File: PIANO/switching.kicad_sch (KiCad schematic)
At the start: 7 parts, among them J3 Barrel_Jack_Switch, U5 AP1509-50SG-13

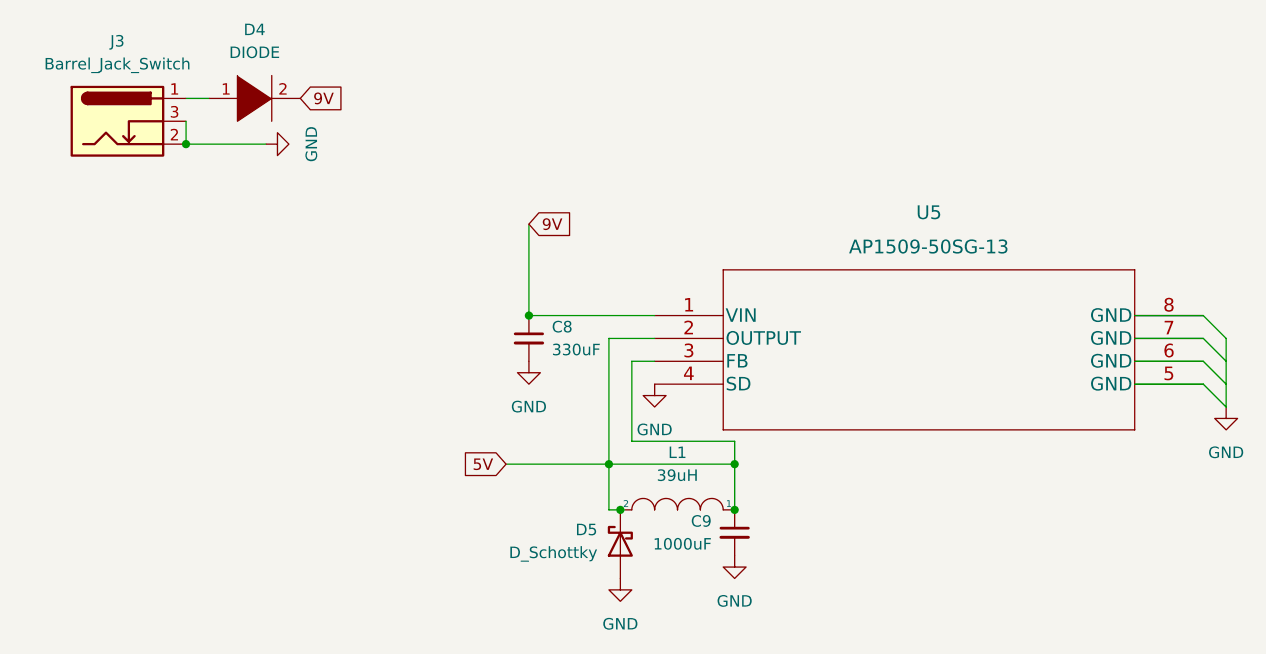
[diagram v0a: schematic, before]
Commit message: Bathroom Trip Commit
Did the circuit for most of the regulator
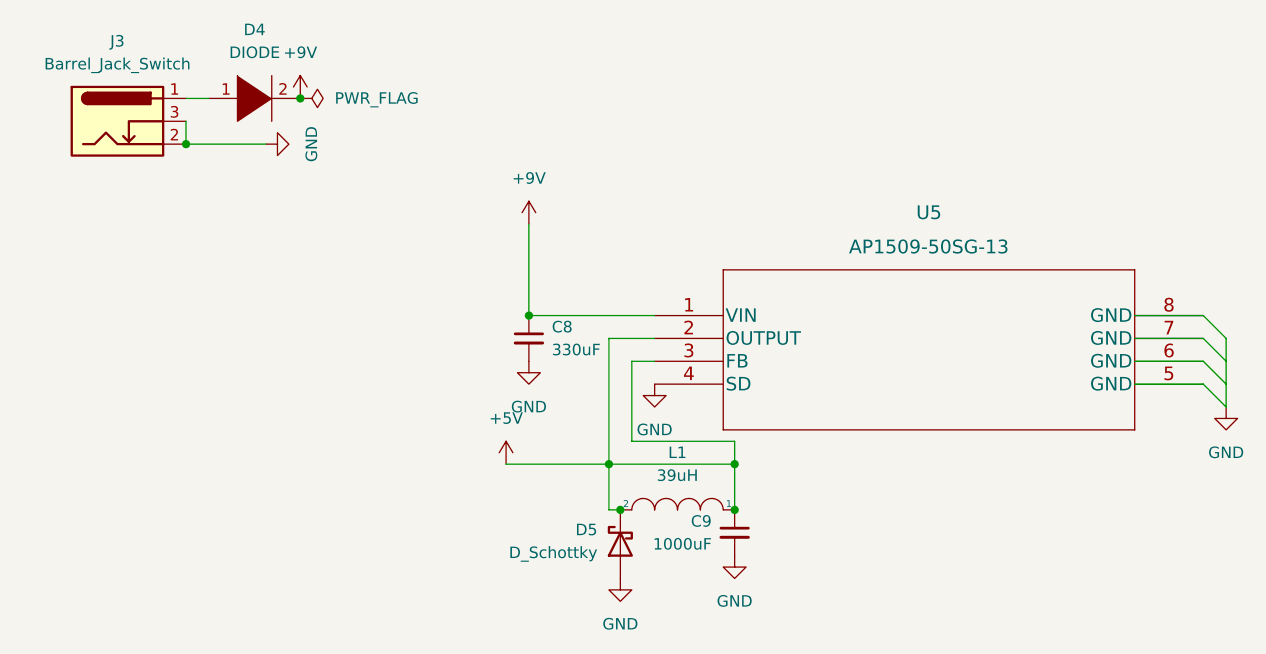
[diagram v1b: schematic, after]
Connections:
- net 5V renamed +5V
- net 9V renamed +9V
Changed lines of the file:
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@@
   (junction (at 129.54 104.14) (diameter 0) (color 0 0 0 0)
   )
+  (junction (at 81.28 58.42) (diameter 0) (color 0 0 0 0)
+  )
   (junction (at 129.54 99.06) (diameter 0) (color 0 0 0 0)
   )
@@
   (wire (pts (xy 129.54 96.52) (xy 118.11 96.52))
     (stroke (width 0) (type default) (color 0 0 0 0))
-  )
-  (global_label "5V" (shape input) (at 104.14 99.06 180) (fields_autoplaced)
-    (effects (font (size 1.27 1.27)) (justify right))
-    (property "Intersheet References" "${INTERSHEET_REFS}" (id 0) (at 99.4288 98.9806 0)
-      (effects (font (size 1.27 1.27)) (justify right) hide)
-    )
-  )
-  (global_label "9V" (shape input) (at 81.28 58.42 0) (fields_autoplaced)
-    (effects (font (size 1.27 1.27)) (justify left))
-    (property "Intersheet References" "${INTERSHEET_REFS}" (id 0) (at 85.9912 58.3406 0)
-      (effects (font (size 1.27 1.27)) (justify left) hide)
-    )
-  )
-  (global_label "9V" (shape input) (at 106.68 72.39 0) (fields_autoplaced)
-    (effects (font (size 1.27 1.27)) (justify left))
-    (property "Intersheet References" "${INTERSHEET_REFS}" (id 0) (at 111.3912 72.3106 0)
-      (effects (font (size 1.27 1.27)) (justify left) hide)
-    )
   )
   (symbol (lib_id "power:GND") (at 77.47 63.5 90) (unit 1)
@@
     )
     (property "Datasheet" "" (id 3) (at 77.47 63.5 0)
+      (effects (font (size 1.27 1.27)) hide)
+    )
+    (pin "1")
+  )
+  (symbol (lib_id "power:PWR_FLAG") (at 81.28 58.42 270) (unit 1)
+    (in_bom yes) (on_board yes) (fields_autoplaced)
+    (property "Reference" "#FLG0104" (id 0) (at 83.185 58.42 0)
+      (effects (font (size 1.27 1.27)) hide)
+    )
+    (property "Value" "PWR_FLAG" (id 1) (at 85.09 58.4199 90)
+      (effects (font (size 1.27 1.27)) (justify left))
+    )
+    (property "Footprint" "" (id 2) (at 81.28 58.42 0)
+      (effects (font (size 1.27 1.27)) hide)
+    )
+    (property "Datasheet" "~" (id 3) (at 81.28 58.42 0)
       (effects (font (size 1.27 1.27)) hide)
     )
@@
     (pin "2")
     (pin "3")
+  )
+  (symbol (lib_id "power:+5V") (at 104.14 99.06 0) (unit 1)
+    (in_bom yes) (on_board yes) (fields_autoplaced)
+    (property "Reference" "#PWR0132" (id 0) (at 104.14 102.87 0)
+      (effects (font (size 1.27 1.27)) hide)
+    )
+    (property "Value" "+5V" (id 1) (at 104.14 93.98 0))
+    (property "Footprint" "" (id 2) (at 104.14 99.06 0)
+      (effects (font (size 1.27 1.27)) hide)
+    )
+    (property "Datasheet" "" (id 3) (at 104.14 99.06 0)
+      (effects (font (size 1.27 1.27)) hide)
+    )
+    (pin "1")
   )
   (symbol (lib_id "power:GND") (at 120.65 90.17 0) (unit 1)
@@
     (pin "8")
   )
+  (symbol (lib_id "power:+9V") (at 81.28 58.42 0) (unit 1)
+    (in_bom yes) (on_board yes) (fields_autoplaced)
+    (property "Reference" "#PWR0136" (id 0) (at 81.28 62.23 0)
+      (effects (font (size 1.27 1.27)) hide)
+    )
+    (property "Value" "+9V" (id 1) (at 81.28 53.34 0))
+    (property "Footprint" "" (id 2) (at 81.28 58.42 0)
+      (effects (font (size 1.27 1.27)) hide)
+    )
+    (property "Datasheet" "" (id 3) (at 81.28 58.42 0)
+      (effects (font (size 1.27 1.27)) hide)
+    )
+    (pin "1")
+  )
   (symbol (lib_id "pspice:INDUCTOR") (at 123.19 104.14 0) (mirror y) (unit 1)
     (in_bom yes) (on_board yes) (fields_autoplaced)
@@
       (effects (font (size 1.27 1.27)) hide)
     )
+    (pin "1")
+  )
+  (symbol (lib_id "power:+9V") (at 106.68 72.39 0) (unit 1)
+    (in_bom yes) (on_board yes) (fields_autoplaced)
+    (property "Reference" "#PWR0137" (id 0) (at 106.68 76.2 0)
+      (effects (font (size 1.27 1.27)) hide)
+    )
+    (property "Value" "+9V" (id 1) (at 106.68 67.31 0))
+    (property "Footprint" "" (id 2) (at 106.68 72.39 0)
+      (effects (font (size 1.27 1.27)) hide)
+    )
+    (property "Datasheet" "" (id 3) (at 106.68 72.39 0)
+      (effects (font (size 1.27 1.27)) hide)
+    )

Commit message: fixed most things
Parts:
- C8: footprint Capacitor_SMD:C_1206_3216Metric -> Capacitor_SMD:C_1210_3225Metric
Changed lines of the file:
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@@
 (kicad_sch (version 20211123) (generator eeschema)
   (paper "A4")
+  (junction (at 106.68 76.2) (diameter 0) (color 0 0 0 0)
+  )
   (junction (at 115.57 99.06) (diameter 0) (color 0 0 0 0)
   )
@@
   (junction (at 106.68 82.55) (diameter 0) (color 0 0 0 0)
   )
+  (junction (at 95.25 96.52) (diameter 0) (color 0 0 0 0)
+  )
   (junction (at 129.54 104.14) (diameter 0) (color 0 0 0 0)
   )
@@
     (stroke (width 0) (type default) (color 0 0 0 0))
   )
-  (wire (pts (xy 106.68 72.39) (xy 106.68 82.55))
+  (wire (pts (xy 106.68 72.39) (xy 106.68 76.2))
     (stroke (width 0) (type default) (color 0 0 0 0))
   )
@@
     (stroke (width 0) (type default) (color 0 0 0 0))
   )
+  (wire (pts (xy 106.68 76.2) (xy 109.22 76.2))
+    (stroke (width 0) (type default) (color 0 0 0 0))
+  )
   (wire (pts (xy 68.58 63.5) (xy 77.47 63.5))
     (stroke (width 0) (type default) (color 0 0 0 0))
@@
     (stroke (width 0) (type default) (color 0 0 0 0))
   )
+  (wire (pts (xy 106.68 76.2) (xy 106.68 82.55))
+    (stroke (width 0) (type default) (color 0 0 0 0))
+  )
   (wire (pts (xy 184.15 90.17) (xy 184.15 92.71))
     (stroke (width 0) (type default) (color 0 0 0 0))
@@
     (stroke (width 0) (type default) (color 0 0 0 0))
   )
-  (wire (pts (xy 104.14 99.06) (xy 115.57 99.06))
+  (wire (pts (xy 95.25 99.06) (xy 115.57 99.06))
     (stroke (width 0) (type default) (color 0 0 0 0))
   )
@@
     (stroke (width 0) (type default) (color 0 0 0 0))
   )
+  (wire (pts (xy 95.25 96.52) (xy 95.25 93.98))
+    (stroke (width 0) (type default) (color 0 0 0 0))
+  )
   (wire (pts (xy 173.99 82.55) (xy 181.61 82.55))
     (stroke (width 0) (type default) (color 0 0 0 0))
   )
+  (wire (pts (xy 95.25 96.52) (xy 97.79 96.52))
+    (stroke (width 0) (type default) (color 0 0 0 0))
+  )
   (wire (pts (xy 129.54 99.06) (xy 129.54 96.52))
     (stroke (width 0) (type default) (color 0 0 0 0))
@@
     (stroke (width 0) (type default) (color 0 0 0 0))
   )
+  (wire (pts (xy 95.25 99.06) (xy 95.25 96.52))
+    (stroke (width 0) (type default) (color 0 0 0 0))
+  )
   (wire (pts (xy 118.11 87.63) (xy 120.65 87.63))
     (stroke (width 0) (type default) (color 0 0 0 0))
@@
   (wire (pts (xy 129.54 96.52) (xy 118.11 96.52))
     (stroke (width 0) (type default) (color 0 0 0 0))
+  )
+  (global_label "9V" (shape input) (at 109.22 76.2 0) (fields_autoplaced)
+    (effects (font (size 1.27 1.27)) (justify left))
+    (property "Intersheet References" "${INTERSHEET_REFS}" (id 0) (at 113.9312 76.1206 0)
+      (effects (font (size 1.27 1.27)) (justify left) hide)
+    )
+  )
+  (global_label "5V" (shape input) (at 97.79 96.52 0) (fields_autoplaced)
+    (effects (font (size 1.27 1.27)) (justify left))
+    (property "Intersheet References" "${INTERSHEET_REFS}" (id 0) (at 102.5012 96.4406 0)
+      (effects (font (size 1.27 1.27)) (justify left) hide)
+    )
   )
   (symbol (lib_id "power:GND") (at 77.47 63.5 90) (unit 1)
@@
     (pin "3")
   )
-  (symbol (lib_id "power:+5V") (at 104.14 99.06 0) (unit 1)
-    (in_bom yes) (on_board yes) (fields_autoplaced)
-    (property "Reference" "#PWR0132" (id 0) (at 104.14 102.87 0)
-      (effects (font (size 1.27 1.27)) hide)
-    )
-    (property "Value" "+5V" (id 1) (at 104.14 93.98 0))
-    (property "Footprint" "" (id 2) (at 104.14 99.06 0)
-      (effects (font (size 1.27 1.27)) hide)
-    )
-    (property "Datasheet" "" (id 3) (at 104.14 99.06 0)
+  (symbol (lib_id "power:+5V") (at 95.25 93.98 0) (unit 1)
+    (in_bom yes) (on_board yes)
+    (property "Reference" "#PWR0132" (id 0) (at 95.25 97.79 0)
+      (effects (font (size 1.27 1.27)) hide)
+    )
+    (property "Value" "+5V" (id 1) (at 92.71 90.17 0))
+    (property "Footprint" "" (id 2) (at 95.25 93.98 0)
+      (effects (font (size 1.27 1.27)) hide)
+    )
+    (property "Datasheet" "" (id 3) (at 95.25 93.98 0)
       (effects (font (size 1.27 1.27)) hide)
     )
@@
   )
   (symbol (lib_id "power:GND") (at 106.68 87.63 0) (unit 1)
-    (in_bom yes) (on_board yes) (fields_autoplaced)
+    (in_bom yes) (on_board yes)
     (property "Reference" "#PWR0130" (id 0) (at 106.68 93.98 0)
       (effects (font (size 1.27 1.27)) hide)
     )
-    (property "Value" "GND" (id 1) (at 106.68 92.71 0))
+    (property "Value" "GND" (id 1) (at 106.68 91.44 0))
     (property "Footprint" "" (id 2) (at 106.68 87.63 0)
       (effects (font (size 1.27 1.27)) hide)
@@
       (effects (font (size 1.27 1.27)) (justify left))
     )
-    (property "Footprint" "Capacitor_SMD:C_1206_3216Metric" (id 2) (at 106.68 85.09 0)
-      (effects (font (size 1.27 1.27)) hide)
-    )
+    (property "Footprint" "Capacitor_SMD:C_1210_3225Metric" (id 2) (at 106.68 85.09 0)
+      (effects (font (size 1.27 1.27)) hide)
+    )
